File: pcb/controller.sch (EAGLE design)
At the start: 90 parts, among them CON1 BINDER-IP40, CON2 BINDER-IP40, IC1 STM32L496X, IC2 TPS62173, IC3 TPS62162, IC4 INA196, IC5 INA196, IC6 INA196, IC7 INA196, Q1 24Mhz, SW1 EC12E_SW, SW2 EC12E_SW, T1 NVR4003NT3G, T2 NVR4003NT3G, T3 IRF7416, T4 IRF7416, T5 NVR4003NT3G, T6 NVR4003NT3G, T7 IRF7416, T8 IRF7416, X1 NEWHAVEN_OLED_256X64, X2 ULTRAFIT-290, X3 PINHD-1X2, X4 NANOFIT-7, X5 PINHD-1X2, X6 NANOFIT-7

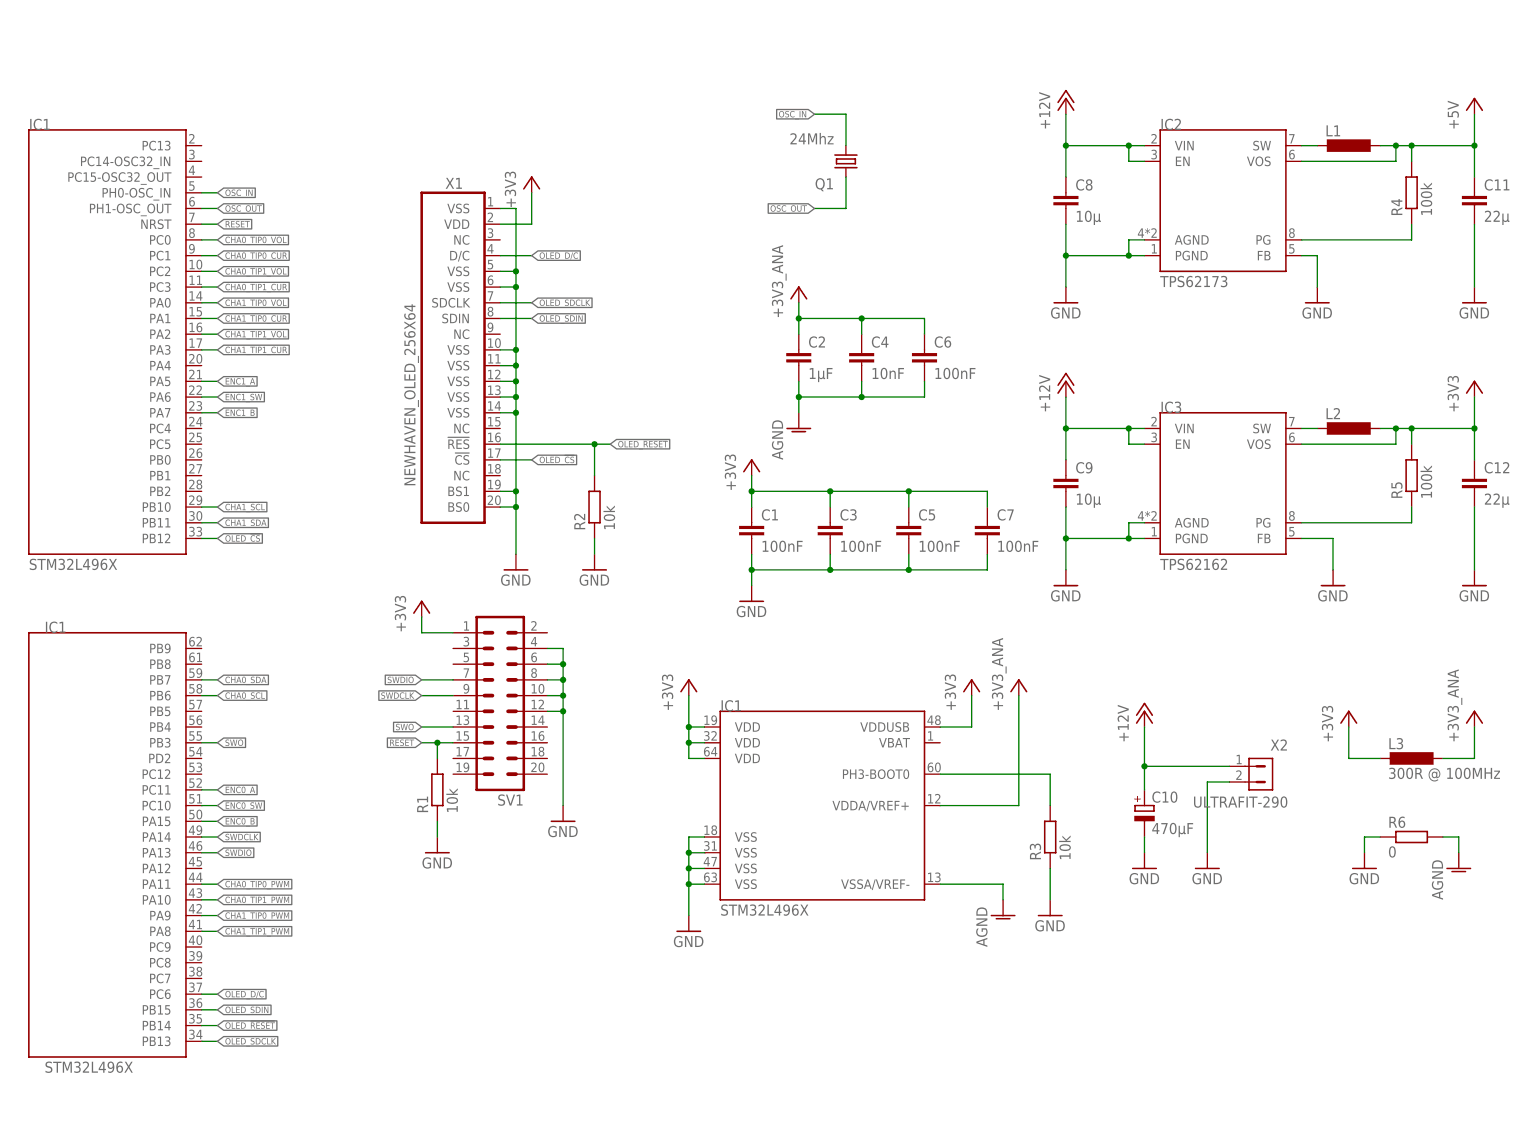
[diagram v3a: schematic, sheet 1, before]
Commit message: iron tweezer updated
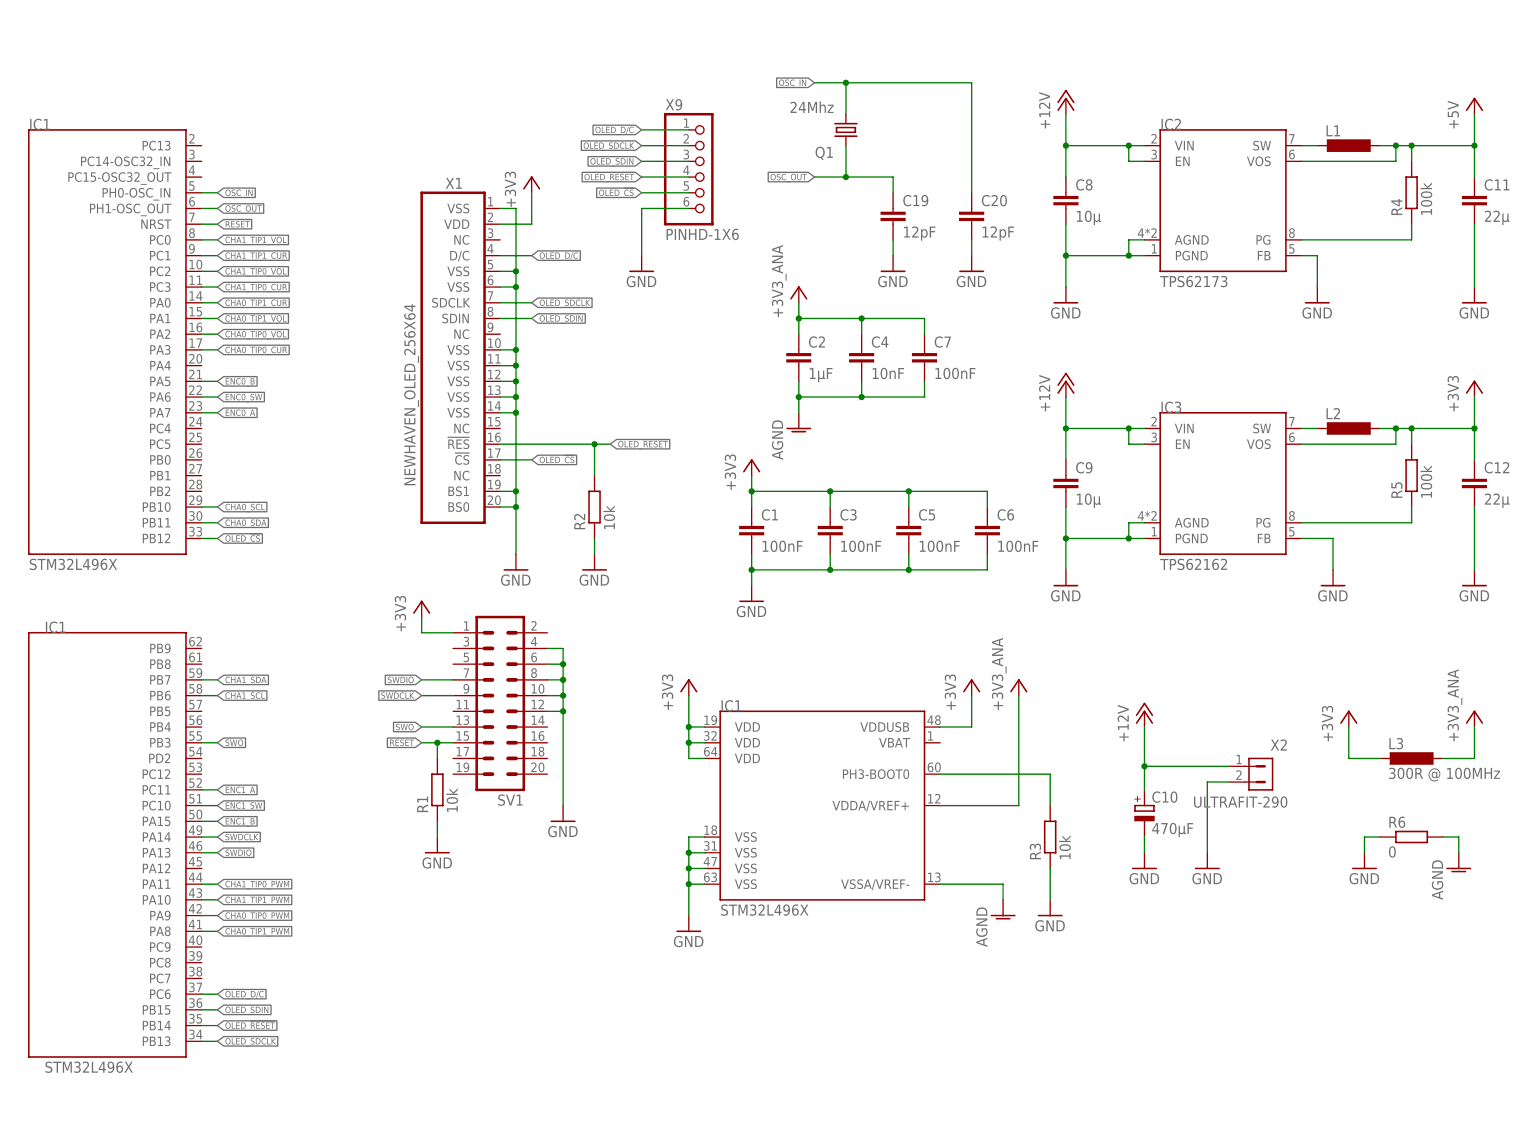
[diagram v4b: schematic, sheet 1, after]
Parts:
- added C19, C20: 12pF, rcl:C-EUC0603
- added X7: PINHD-1X4, solderpi:PINHD-1X4
- added X8: PINHD-1X3, solderpi:PINHD-1X3
- added X9: PINHD-1X6, solderpi:PINHD-1X6
- C1, C3, C5, C6, C7: device rcl:C-EUC0603 -> rcl:C-EUC0402; OC_DIGIKEY 1276-1005-1-ND -> 1276-1001-1-ND
- C10: OC_DIGIKEY (none) -> PCE3805CT-ND; OC_MOUSER 667-EEE-FK1E471P -> (none)
- C13, C14, C16, C17: OC_DIGIKEY (none) -> 732-8061-1-ND; OC_MOUSER 710-885012207072 -> (none)
- C15, C18: OC_DIGIKEY (none) -> 399-8008-1-ND; OC_MOUSER 80-C0805C105M3R -> (none)
- C2: device rcl:C-EUC0603 -> rcl:C-EUC0402; OC_DIGIKEY 1276-1034-1-ND -> 1276-1067-1-ND
- C4: device rcl:C-EUC0603 -> rcl:C-EUC0402; OC_DIGIKEY 478-6209-1-ND -> 311-1042-1-ND
- R17, R18, R20, R22, R23, R35, R37, R39, R40, R41: OC_DIGIKEY (none) -> 311-10.0KCRCT-ND; OC_MOUSER 603-RC0805FR-0710KL -> (none)
- R24, R42: OC_DIGIKEY (none) -> 311-22.0KCRCT-ND; OC_MOUSER 603-RC0805FR-0722KL -> (none)
- SV1: OC_DIGIKEY (none) -> S9172-ND
- X1: OC_DIGIKEY (none) -> SAM1093-20-ND
- X2: OC_DIGIKEY (none) -> WM11586-ND
- X3: value PINHD-1X2 -> PINHD-1X3; device solderpi:PINHD-1X2 -> solderpi:PINHD-1X3; OC_DIGIKEY (none) -> 1849-1003-ND; OC_MOUSER 855-M20-9990246 -> (none)
- X4, X6: OC_DIGIKEY (none) -> WM16898-ND; OC_MOUSER 538-105313-1107, 538-105307-1207 -> (none)
- X5: value PINHD-1X2 -> PINHD-1X4; device solderpi:PINHD-1X2 -> solderpi:PINHD-1X4; OC_DIGIKEY (none) -> 2057-PH1-04-UA-ND; OC_MOUSER 855-M20-9990246 -> (none)
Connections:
- net N$37 renamed BOOT0
- net +3V3: now also C6.1, R40.2; no longer C7.1, R23.2
- net +3V3_ANA: now also C7.1; no longer C6.1
- net AGND: now also C7.2; no longer C6.2
- net CHA0_SCL: now also IC1G$1.PB10, X8.1; no longer IC1G$2.PB6, X3.1
- net CHA0_SDA: now also IC1G$1.PB11, X8.2; no longer IC1G$2.PB7, X3.2
- net CHA0_TIP0_CUR: now also IC1G$1.PA3; no longer IC1G$1.PC1
- net CHA0_TIP0_PWM: now also IC1G$2.PA9; no longer IC1G$2.PA11
- net CHA0_TIP0_VOL: now also IC1G$1.PA2; no longer IC1G$1.PC0
- net CHA0_TIP1_CUR: now also IC1G$1.PA0; no longer IC1G$1.PC3
- net CHA0_TIP1_PWM: now also IC1G$2.PA8; no longer IC1G$2.PA10
- net CHA0_TIP1_VOL: now also IC1G$1.PA1; no longer IC1G$1.PC2
- net CHA1_SCL: now also IC1G$2.PB6, X3.1; no longer IC1G$1.PB10, X5.1
- net CHA1_SDA: now also IC1G$2.PB7, X3.2; no longer IC1G$1.PB11, X5.2
- net CHA1_TIP0_CUR: now also IC1G$1.PC3; no longer IC1G$1.PA1
- net CHA1_TIP0_PWM: now also IC1G$2.PA11; no longer IC1G$2.PA9
- net CHA1_TIP0_VOL: now also IC1G$1.PC2; no longer IC1G$1.PA0
- net CHA1_TIP1_CUR: now also IC1G$1.PC1; no longer IC1G$1.PA3
- net CHA1_TIP1_PWM: now also IC1G$2.PA10; no longer IC1G$2.PA8
- net CHA1_TIP1_VOL: now also IC1G$1.PC0; no longer IC1G$1.PA2
- net ENC0_A: now also IC1G$1.PA7, X7.1; no longer IC1G$2.PC11
- net ENC0_B: now also IC1G$1.PA5, R22.1, X7.3; no longer IC1G$2.PA15, R22.2
- net ENC0_B_UNFIL: now also R22.2; no longer R22.1
- net ENC0_SW: now also IC1G$1.PA6, X7.2; no longer IC1G$2.PC10
- net ENC0_SW_R: now also R41.1; no longer R23.1
- net ENC1_A: now also IC1G$2.PC11, R23.1, X5.2; no longer IC1G$1.PA5, R35.1
- net ENC1_A_UNFIL: now also R23.2; no longer R35.2
- net ENC1_B: now also IC1G$2.PA15, R35.2, X5.4; no longer IC1G$1.PA7, R40.2
- net ENC1_B_UNFIL: now also R35.1; no longer R40.1
- net ENC1_SW: now also IC1G$2.PC10, X5.3; no longer IC1G$1.PA6
- net ENC1_SW_R: now also R40.1; no longer R41.1
- net GND: now also C19.2, C20.2, C6.2, X3.3, X5.1, X7.4, X8.3, X9.6; no longer C7.2
- net OLED_!CS: now also X9.5
- net OLED_!RESET: now also X9.4
- net OLED_D/C: now also X9.1
- net OLED_SDCLK: now also X9.2
- net OLED_SDIN: now also X9.3
- net OSC_IN: now also C20.1
- net OSC_OUT: now also C19.1
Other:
- moved on the sheet: C6, C7, Q1, R22, R35, R40

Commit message: boms reworked
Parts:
- removed C11: 22µ, rcl:C-EUC0805
- removed C8: 10µ, rcl:C-EUC0805
- removed IC2: TPS62173, solderpi:TPS62173
- removed L1: (no value), solderpi:VLF3012S
- removed L3: 300R @ 100MHz, solderpi:L0603
- removed R4: 100k, rcl:R-EU_R0603
- removed R6: 0, rcl:R-EU_R2010
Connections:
- removed net +3V3_ANA: C2.1, C4.1, C7.1, IC1G$3.VDDA/VREF+, IC4.V+, IC5.V+, IC6.V+, IC7.V+, L3.1
- removed net +5V: C11.1, IC2.VOS, L1.1, R19.2, R21.2, R36.2, R38.2, R4.2, X4.3, X6.3
- removed net 5V_PG: IC2.PG, R4.1
- removed net 5V_SW: IC2.SW, L1.2
- removed net AGND: C2.2, C4.2, C7.2, IC1G$3.VSSA/VREF-, IC4.GND, IC5.GND, IC6.GND, IC7.GND, R6.2
- net +12V: no longer C8.1, IC2.EN, IC2.VIN
- net +3V3: now also C2.1, C4.1, C7.1, IC1G$3.VDDA/VREF+, IC4.V+, IC5.V+, IC6.V+, IC7.V+, R19.2, R21.2, R36.2, R38.2, X4.3, X6.3; no longer L3.2
- net CHA1_TIP1_CUR: now also IC1G$1.PC0; no longer IC1G$1.PC1
- net CHA1_TIP1_VOL: now also IC1G$1.PC1; no longer IC1G$1.PC0
- net GND: now also C2.2, C4.2, C7.2, IC1G$3.VSSA/VREF-, IC4.GND, IC5.GND, IC6.GND, IC7.GND; no longer C11.2, C8.2, IC2.AGND, IC2.FB, IC2.PGND, R6.1
